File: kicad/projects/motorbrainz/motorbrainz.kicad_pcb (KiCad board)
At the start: 4 copper layers, 69.9 x 31.8 mm, 40 parts, among them J1 FTSH-105-01-S-DV-K, J2 FTSH-105-01-S-DV-K, J3 Screw_Terminal_01x02, J4 Screw_Terminal_01x02, J5 Screw_Terminal_01x02, J6 Conn_01x03_MountingPin, J7 FTSH-105-01-S-DV-K, U1 tinyPICO_Nano, U10 CDBA240LL-HF, U11 LD1117S50TR_SOT223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

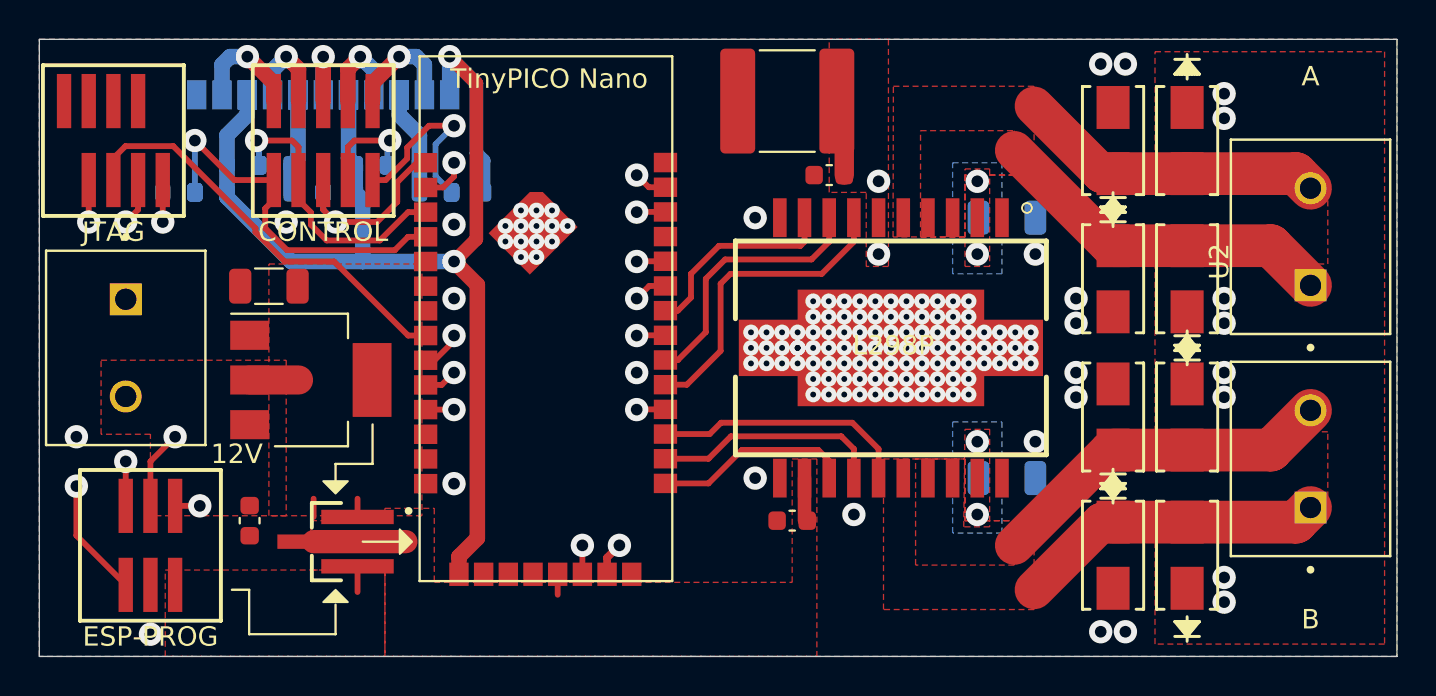
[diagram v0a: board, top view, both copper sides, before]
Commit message: 2.0: replace ESP-PROG with USB connecter to use TinyPICO NANO USB to serial converter
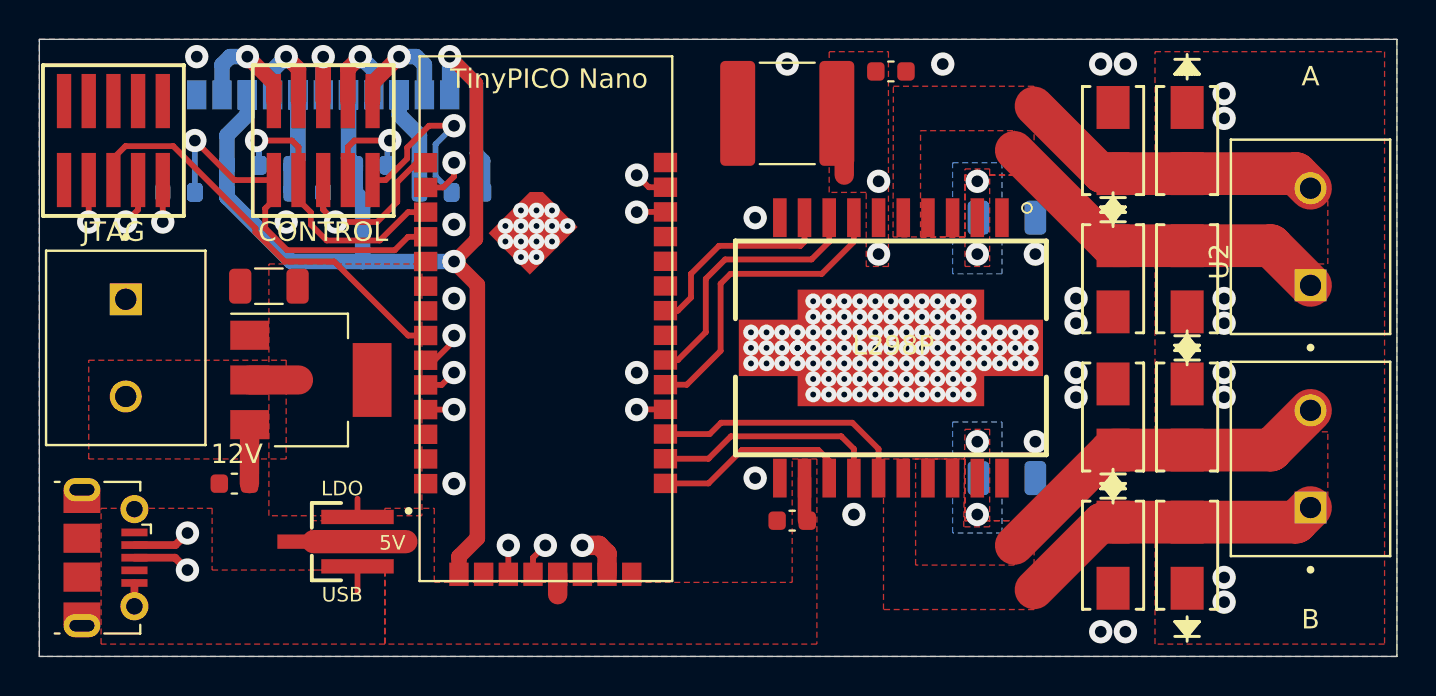
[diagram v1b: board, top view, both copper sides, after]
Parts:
- J2: value FTSH-105-01-S-DV-K -> USB_B_Micro; footprint snapeda:SAMTEC-FTSH-105-01-X-DV -> Connector_USB:USB_Micro-B_Molex-105017-0001
- moved C4 6.21 mm to (135.9, 87.4), turned to 0 degrees
- moved J2 2.37 mm to (95.5, 112.4), turned to 270 degrees
- moved C1 2.06 mm to (102.1, 108.6), turned to 180 degrees
- moved C5 0.63 mm to (130.6, 89.5)
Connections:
- J2 pad 3: /RESET -> /D+
- J2 pad 4: /+5VFAR -> Net-(J2-Pad4)
- J2 pad 5: /TXD -> GND
- U1 pad 1: (no net) -> Net-(U1-Pad1)
- U1 pad 10: (no net) -> Net-(U1-Pad10)
- U1 pad 11: (no net) -> Net-(U1-Pad11)
- U1 pad 16: (no net) -> Net-(U1-Pad16)
- U1 pad 17: (no net) -> Net-(U1-Pad17)
- U1 pad 18: (no net) -> Net-(U1-Pad18)
- U1 pad 33: (no net) -> Net-(U1-Pad33)
- U1 pad 36: (no net) -> Net-(U1-Pad36)
- U1 pad 5: (no net) -> /D-
- U1 pad 6: (no net) -> /D+
- U1 pad 7: (no net) -> Net-(U1-Pad7)
- U1 pad 9: (no net) -> Net-(U1-Pad9)
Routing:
- net /IO0: track 40.4 -> 0.00 mm, vias 2 -> 0
- net /RXD: track 33.8 -> 0.00 mm, vias 2 -> 0
- net /TXD: track 33.0 -> 0.00 mm, vias 2 -> 0
- net /D-: track 0.00 -> 23.9 mm, vias 0 -> 2
- net /RESET: track 23.3 -> 0.00 mm, vias 2 -> 0
- net /D+: track 0.00 -> 21.5 mm, vias 0 -> 2
- net +12V: track 3.97 -> 7.00 mm
- net GND: track 12.4 -> 14.3 mm, vias 137 -> 138
- net /+5VNEAR: track 4.39 -> 3.45 mm
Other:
- board text added: "5V"
- board text added: "For wired switches: Pull up (◀, +3V3) or down (▷, GND) an open switch with a resistor. Bridge other side, respectively, down (▶, GND) or up (◁, +3V3) to affect change when switch is closed."
- board text added: "LDO"
- board text added: "USB"
- board text added: "motorbrainz 2.0 © 2021 Ross Tyler"
- board text removed: "- IO0 GND +5V -"
- board text removed: "- RXD TXD RESET -"
- board text removed: "ESP-PROG"
- board text removed: "For wired switches: Pull up (◀, +3V3) or down (▷, GND) an open switch with a resistor. Bridge other side down (▶, GND) or up (◁, +3V3) to affect change when switch is closed."
- board text removed: "motorbrainz 1.0 © 2021 Ross Tyler"

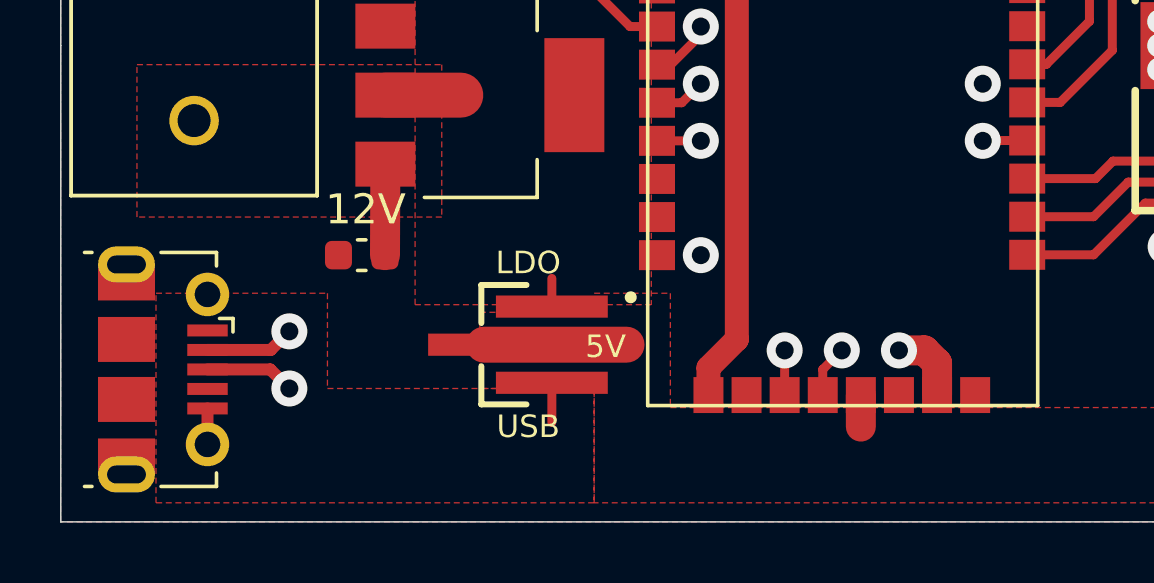
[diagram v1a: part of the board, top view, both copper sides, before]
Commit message: thicken USB power traces
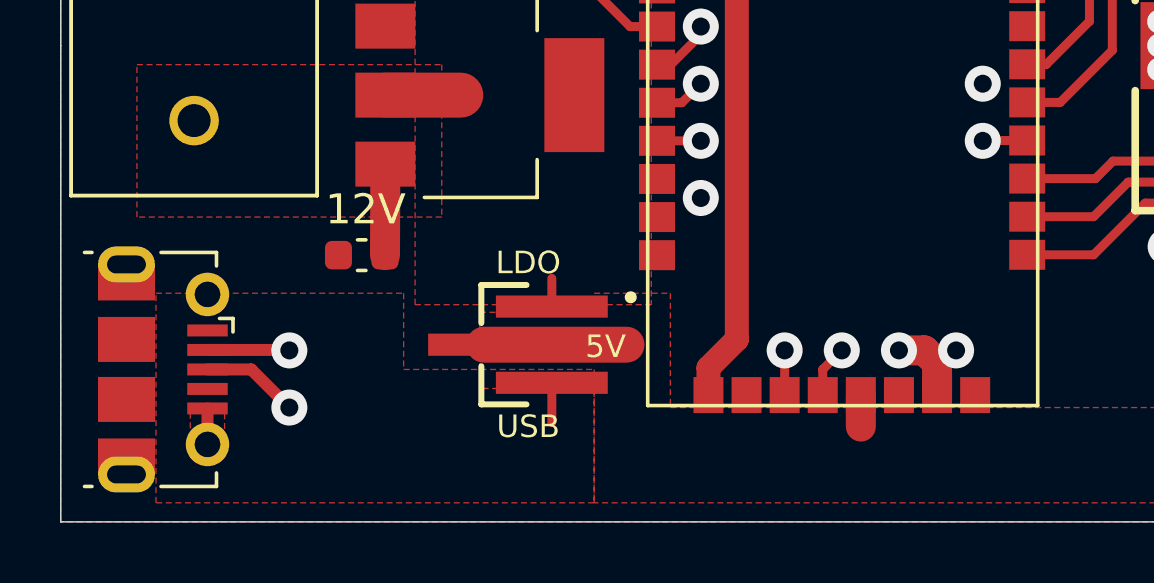
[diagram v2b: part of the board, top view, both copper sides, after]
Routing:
- net /D+: track 21.5 -> 22.0 mm
- net GND: vias 138 -> 139
